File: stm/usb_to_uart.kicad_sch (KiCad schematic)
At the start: 8 parts, among them U6 FT232RL

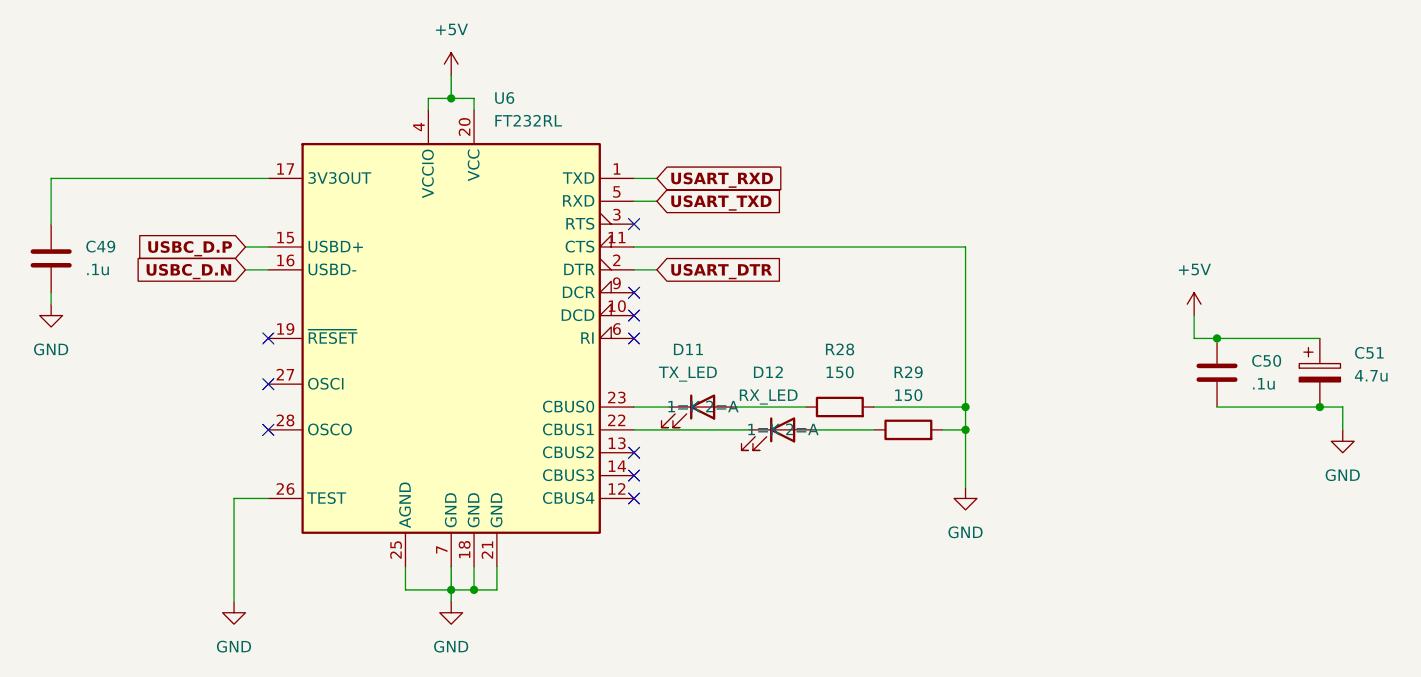
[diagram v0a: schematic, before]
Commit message: usb to uart fix
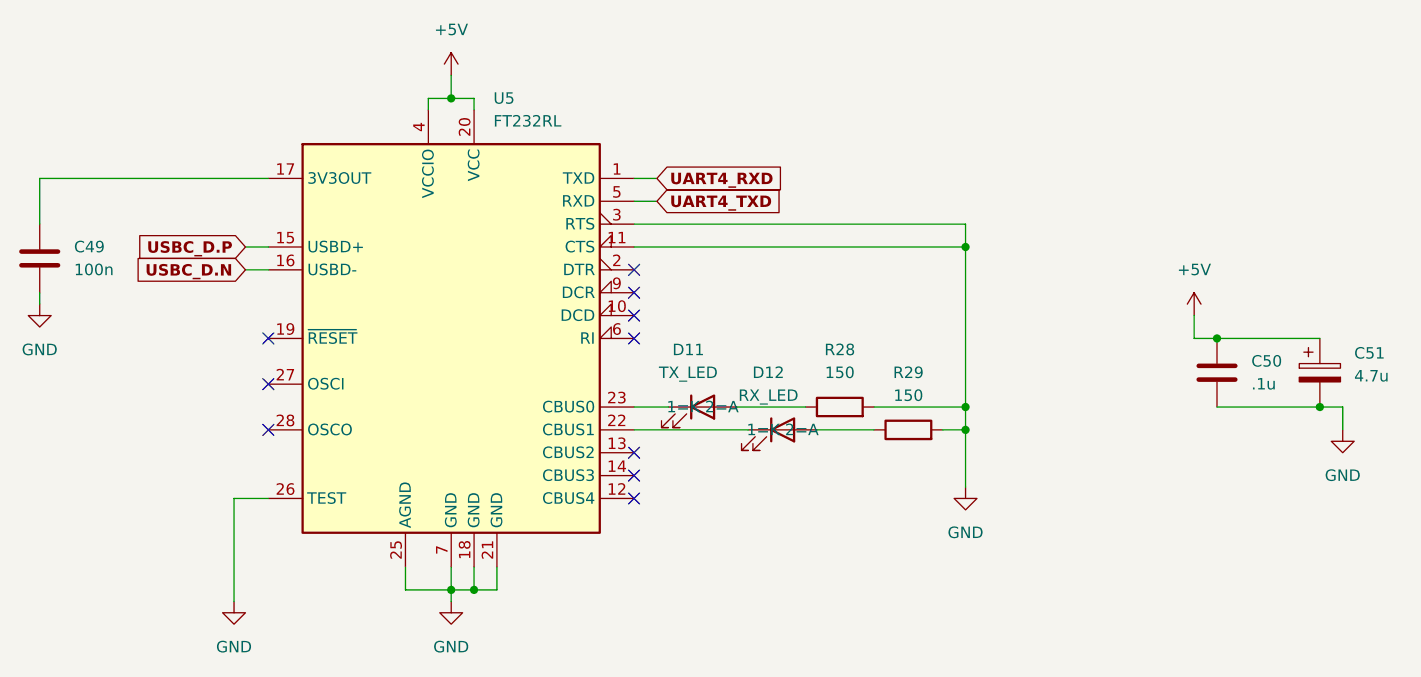
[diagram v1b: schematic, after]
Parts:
- removed U6: FT232RL, Package_SO:SSOP-28_5.3x10.2mm_P0.65mm, symbol Interface_USB:FT232RL
- added U5: FT232RL, Package_SO:SSOP-28_5.3x10.2mm_P0.65mm, symbol Interface_USB:FT232RL
- C49: value .1u -> 100n
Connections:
- net +5V: now also U5.20 (VCC), U5.4 (VCCIO)
- net GND: now also U5.11 (CTS), U5.18 (GND), U5.21 (GND), U5.25 (AGND), U5.26 (TEST), U5.3 (RTS), U5.7 (GND)
- net USBC_D.N: now also U5.16 (USBD-)
- net USBC_D.P: now also U5.15 (USBD+)
- net at C49.1: now also U5.17 (3V3OUT)
- net at D12.1 (K): now also U5.22 (CBUS1)
- net at D11.1 (K): now also U5.23 (CBUS0)
- new net UART4_RXD: U5.1 (TXD)
- new net UART4_TXD: U5.5 (RXD)
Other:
- moved on the sheet: C49
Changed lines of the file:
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@@
+	)
+	(junction
+		(at 162.56 64.77)
+		(diameter 0)
+		(color 0 0 0 0)
 	)
 	(junction
@@
 	)
 	(no_connect
+		(at 125.73 67.31)
+	)
+	(no_connect
 		(at 125.73 72.39)
 	)
@@
 	)
 	(no_connect
-		(at 125.73 62.23)
-	)
-	(no_connect
 		(at 85.09 74.93)
 	)
@@
 	(wire
 		(pts
-			(xy 60.96 57.15) (xy 85.09 57.15)
+			(xy 59.69 57.15) (xy 85.09 57.15)
 		)
 		(stroke
@@
 	(wire
 		(pts
+			(xy 162.56 62.23) (xy 162.56 64.77)
+		)
+		(stroke
+			(width 0)
+			(type default)
+		)
+	)
+	(wire
+		(pts
+			(xy 125.73 62.23) (xy 162.56 62.23)
+		)
+		(stroke
+			(width 0)
+			(type default)
+		)
+	)
+	(wire
+		(pts
 			(xy 81.28 104.14) (xy 81.28 92.71)
 		)
@@
 	(wire
 		(pts
-			(xy 125.73 67.31) (xy 128.27 67.31)
-		)
-		(stroke
-			(width 0)
-			(type default)
-		)
-	)
-	(wire
-		(pts
 			(xy 162.56 64.77) (xy 162.56 82.55)
 		)
@@
 	(wire
 		(pts
-			(xy 60.96 71.12) (xy 60.96 69.85)
+			(xy 59.69 71.12) (xy 59.69 69.85)
 		)
 		(stroke
@@
 	(wire
 		(pts
-			(xy 60.96 62.23) (xy 60.96 57.15)
+			(xy 59.69 62.23) (xy 59.69 57.15)
 		)
 		(stroke
@@
 		)
 	)
-	(global_label "USART_RXD"
+	(global_label "UART4_RXD"
 		(shape input)
 		(at 128.27 57.15 0)
@@
 		)
 	)
-	(global_label "USART_TXD"
+	(global_label "UART4_TXD"
 		(shape input)
 		(at 128.27 59.69 0)
@@
 				)
 				(justify right)
-				(hide yes)
-			)
-		)
-	)
-	(global_label "USART_DTR"
-		(shape input)
-		(at 128.27 67.31 0)
-		(fields_autoplaced yes)
-		(effects
-			(font
-				(size 1.27 1.27)
-				(thickness 0.254)
-				(bold yes)
-			)
-			(justify left)
-		)
-		(property "Intersheetrefs" "${INTERSHEET_REFS}"
-			(at 142.0726 67.31 0)
-			(effects
-				(font
-					(size 1.27 1.27)
-				)
-				(justify left)
 				(hide yes)
 			)
@@
 	)
 	(symbol
-		(lib_id "Interface_USB:FT232RL")
-		(at 105.41 74.93 0)
+		(lib_id "power:GND")
+		(at 59.69 71.12 0)
 		(unit 1)
 		(exclude_from_sim no)
@@
 		(dnp no)
 		(fields_autoplaced yes)
-		(property "Reference" "U6"
-			(at 110.1441 48.26 0)
-			(effects
-				(font
-					(size 1.27 1.27)
-				)
-				(justify left)
-			)
-		)
-		(property "Value" "FT232RL"
-			(at 110.1441 50.8 0)
-			(effects
-				(font
-					(size 1.27 1.27)
-				)
-				(justify left)
-			)
-		)
-		(property "Footprint" "Package_SO:SSOP-28_5.3x10.2mm_P0.65mm"
-			(at 133.35 97.79 0)
-			(effects
-				(font
-					(size 1.27 1.27)
-				)
-				(hide yes)
-			)
-		)
-		(property "Datasheet" "https://www.ftdichip.com/Support/Documents/DataSheets/ICs/DS_FT232R.pdf"
-			(at 105.41 74.93 0)
-			(effects
-				(font
-					(size 1.27 1.27)
-				)
-				(hide yes)
-			)
-		)
-		(property "Description" "USB to Serial Interface, SSOP-28"
-			(at 105.41 74.93 0)
-			(effects
-				(font
-					(size 1.27 1.27)
-				)
-				(hide yes)
-			)
-		)
-		(pin "12"
-		)
-		(pin "22"
-		)
-		(pin "20"
-		)
-		(pin "6"
-		)
-		(pin "2"
-		)
-		(pin "3"
-		)
-		(pin "28"
-		)
-		(pin "7"
-		)
-		(pin "26"
-		)
-		(pin "13"
-		)
-		(pin "23"
-		)
-		(pin "19"
-		)
-		(pin "10"
-		)
-		(pin "21"
-		)
-		(pin "18"
-		)
-		(pin "14"
-		)
-		(pin "4"
-		)
-		(pin "25"
-		)
-		(pin "16"
-		)
-		(pin "9"
-		)
-		(pin "17"
-		)
-		(pin "11"
-		)
-		(pin "1"
-		)
-		(pin "15"
-		)
-		(pin "5"
-		)
-		(pin "27"
-		)
-		(instances
-			(project "stm"
-				(path "/8c38e4ab-00b4-41d2-ba83-c24ee9e4f60d/f758c19f-a19d-4214-8717-e2817252528b"
-					(reference "U6")
-					(unit 1)
-				)
-			)
-		)
-	)
-	(symbol
-		(lib_id "power:GND")
-		(at 60.96 71.12 0)
-		(unit 1)
-		(exclude_from_sim no)
-		(in_bom yes)
-		(on_board yes)
-		(dnp no)
-		(fields_autoplaced yes)
 		(property "Reference" "#PWR059"
-			(at 60.96 77.47 0)
+			(at 59.69 77.47 0)
 			(effects
 				(font
@@
 		)
 		(property "Value" "GND"
-			(at 60.96 76.2 0)
+			(at 59.69 76.2 0)
 			(effects
 				(font
@@
 		)
 		(property "Footprint" ""
-			(at 60.96 71.12 0)
+			(at 59.69 71.12 0)
 			(effects
 				(font
@@
 		)
 		(property "Datasheet" ""
-			(at 60.96 71.12 0)
+			(at 59.69 71.12 0)
 			(effects
 				(font
@@
 		)
 		(property "Description" "Power symbol creates a global label with name \"GND\" , ground"
-			(at 60.96 71.12 0)
+			(at 59.69 71.12 0)
 			(effects
 				(font
@@
 	)
 	(symbol
-		(lib_id "Device:C")
-		(at 60.96 66.04 0)
+		(lib_id "Interface_USB:FT232RL")
+		(at 105.41 74.93 0)
 		(unit 1)
 		(exclude_from_sim no)
@@
 		(dnp no)
 		(fields_autoplaced yes)
+		(property "Reference" "U5"
+			(at 110.0933 48.26 0)
+			(effects
+				(font
+					(size 1.27 1.27)
+				)
+				(justify left)
+			)
+		)
+		(property "Value" "FT232RL"
+			(at 110.0933 50.8 0)
+			(effects
+				(font
+					(size 1.27 1.27)
+				)
+				(justify left)
+			)
+		)
+		(property "Footprint" "Package_SO:SSOP-28_5.3x10.2mm_P0.65mm"
+			(at 133.35 97.79 0)
+			(effects
+				(font
+					(size 1.27 1.27)
+				)
+				(hide yes)
+			)
+		)
+		(property "Datasheet" "https://www.ftdichip.com/Support/Documents/DataSheets/ICs/DS_FT232R.pdf"
+			(at 105.41 74.93 0)
+			(effects
+				(font
+					(size 1.27 1.27)
+				)
+				(hide yes)
+			)
+		)
+		(property "Description" "USB to Serial Interface, SSOP-28"
+			(at 105.41 74.93 0)
+			(effects
+				(font
+					(size 1.27 1.27)
+				)
+				(hide yes)
+			)
+		)
+		(pin "19"
+		)
+		(pin "18"
+		)
+		(pin "11"
+		)
+		(pin "7"
+		)
+		(pin "1"
+		)
+		(pin "16"
+		)
+		(pin "28"
+		)
+		(pin "9"
+		)
+		(pin "27"
+		)
+		(pin "17"
+		)
+		(pin "26"
+		)
+		(pin "15"
+		)
+		(pin "25"
+		)
+		(pin "4"
+		)
+		(pin "20"
+		)
+		(pin "5"
+		)
+		(pin "21"
+		)
+		(pin "3"
+		)
+		(pin "2"
+		)
+		(pin "10"
+		)
+		(pin "22"
+		)
+		(pin "13"
+		)
+		(pin "12"
+		)
+		(pin "23"
+		)
+		(pin "14"
+		)
+		(pin "6"
+		)
+		(instances
+			(project ""
+				(path "/8c38e4ab-00b4-41d2-ba83-c24ee9e4f60d/f758c19f-a19d-4214-8717-e2817252528b"
+					(reference "U5")
+					(unit 1)
+				)
+			)
+		)
+	)
+	(symbol
+		(lib_id "Device:C")
+		(at 59.69 66.04 0)
+		(unit 1)
+		(exclude_from_sim no)
+		(in_bom yes)
+		(on_board yes)
+		(dnp no)
+		(fields_autoplaced yes)
 		(property "Reference" "C49"
-			(at 64.77 64.7699 0)
+			(at 63.5 64.7699 0)
 			(effects
 				(font
@@
 			)
 		)
-		(property "Value" ".1u"
-			(at 64.77 67.3099 0)
+		(property "Value" "100n"
+			(at 63.5 67.3099 0)
 			(effects
 				(font
@@
 		)
 		(property "Footprint" "Capacitor_SMD:C_0603_1608Metric"
-			(at 61.9252 69.85 0)
+			(at 60.6552 69.85 0)
 			(effects
 				(font
@@
 		)
 		(property "Datasheet" "~"
-			(at 60.96 66.04 0)
+			(at 59.69 66.04 0)
 			(effects
 				(font
@@
 		)
 		(property "Description" "Unpolarized capacitor"
-			(at 60.96 66.04 0)
-			(effects
-				(font
+			(at 59.69 66.04 0)
+			(effects
+				(font
